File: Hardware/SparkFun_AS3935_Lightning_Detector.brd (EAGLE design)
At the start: 25.4 x 25.4 mm, 57 parts, among them U1 AS3935

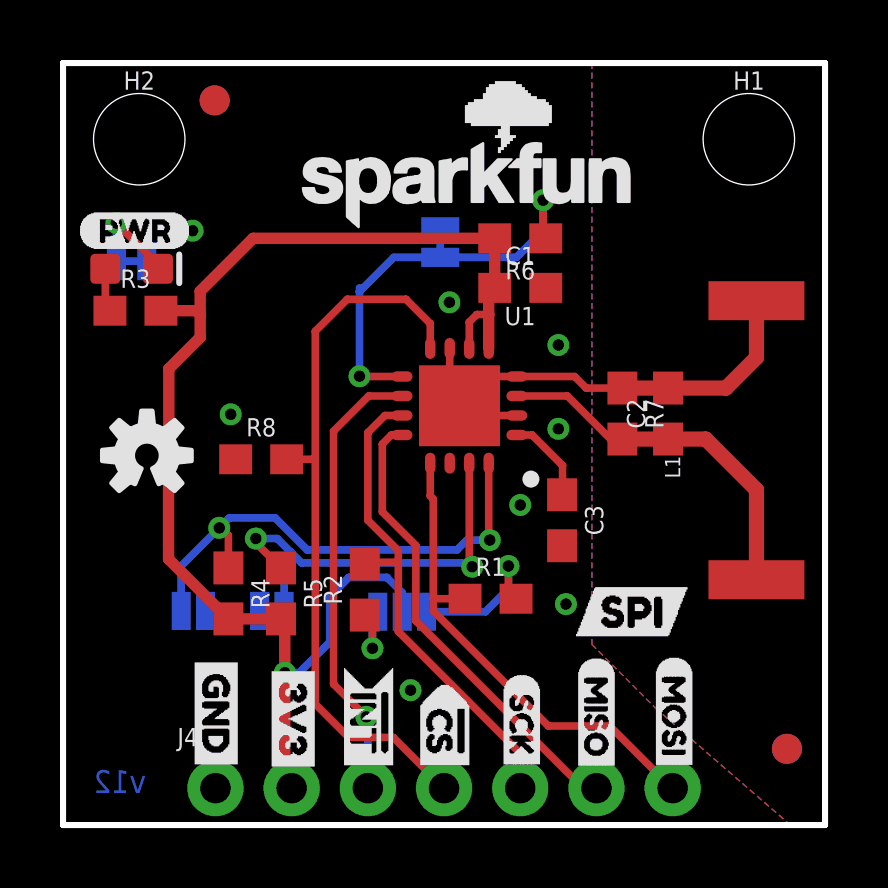
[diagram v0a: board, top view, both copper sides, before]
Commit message: Updates jumper on underside to read I2C rather than SPI
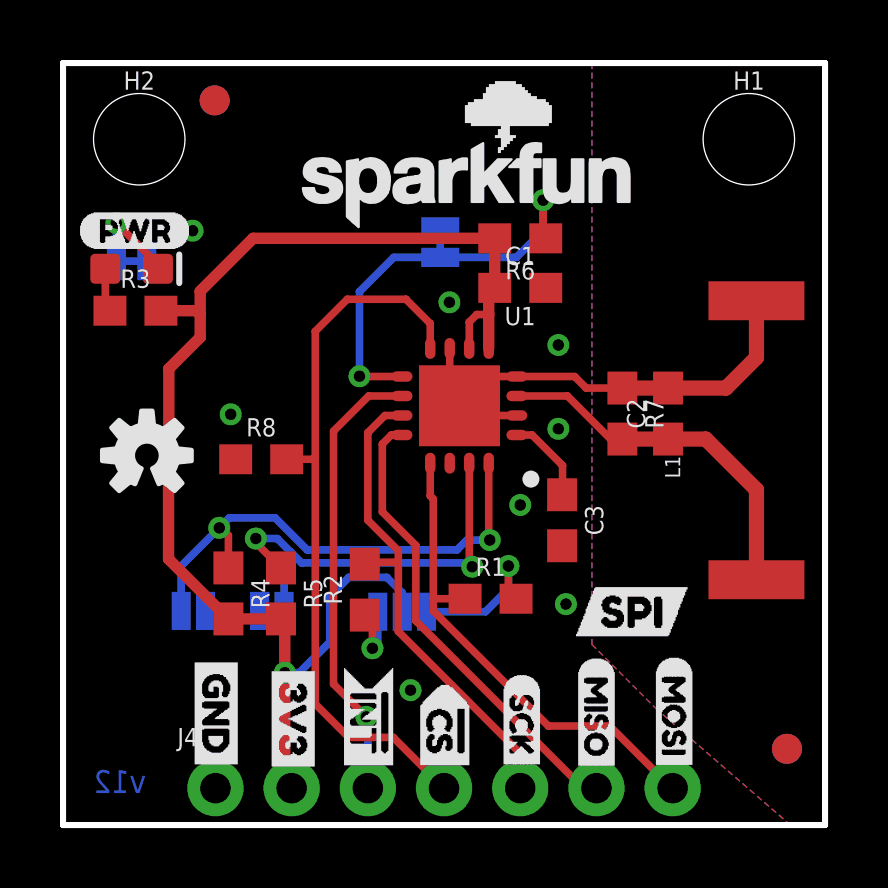
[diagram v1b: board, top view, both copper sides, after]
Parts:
- removed U$35: (no value), SPI:SPI0
- added U$16: (no value), Labels:I_SUPER2_C-()-04
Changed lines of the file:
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@@
 <layer number="19" name="Unrouted" color="6" fill="1" visible="yes" active="yes"/>
 <layer number="20" name="Dimension" color="15" fill="1" visible="yes" active="yes"/>
-<layer number="21" name="tPlace" color="16" fill="1" visible="no" active="yes"/>
-<layer number="22" name="bPlace" color="14" fill="1" visible="no" active="yes"/>
+<layer number="21" name="tPlace" color="16" fill="1" visible="yes" active="yes"/>
+<layer number="22" name="bPlace" color="14" fill="1" visible="yes" active="yes"/>
 <layer number="23" name="tOrigins" color="15" fill="1" visible="yes" active="yes"/>
 <layer number="24" name="bOrigins" color="15" fill="1" visible="yes" active="yes"/>
@@
 <element name="U$33" library="Labels" package="ADR-()-04" value="" x="7.9502" y="9.1694" smashed="yes" rot="MR0"/>
 <element name="U$34" library="PULLUP" package="I#C_PU0" value="" x="14.2494" y="9.144" smashed="yes" rot="MR0"/>
-<element name="U$35" library="SPI" package="SPI0" value="" x="14.605" y="21.717" smashed="yes" rot="MR0"/>
 <element name="U$36" library="one" package="10" value="" x="3.9878" y="7.0866" smashed="yes" rot="MR0"/>
 <element name="U$37" library="zero" package="00" value="" x="9.9822" y="7.1374" smashed="yes" rot="MR0"/>
@@
 <element name="U$14" library="INT" package="#INT0" value="" x="10.1854" y="5.5118" smashed="yes" rot="MR270"/>
 <element name="U$15" library="DataLines" package="SPI1" value="" x="21.082" y="7.112" smashed="yes" rot="MR0"/>
+<element name="U$16" library="Labels" package="I_SUPER2_C-()-04" value="" x="14.5034" y="21.6662" smashed="yes" rot="MR0"/>
 </elements>
 <signals>
@@
 <contactref element="U1" pad="9"/>
 <via x="16.002" y="20.828" extent="1-16" drill="0.381"/>
-<wire x1="15.2146" y1="19.0246" x2="15.24" y2="19.05" width="0.254" layer="16"/>
-<wire x1="15.24" y1="19.05" x2="16.002" y2="19.812" width="0.254" layer="16"/>
+<wire x1="15.113" y1="18.923" x2="16.002" y2="19.812" width="0.254" layer="16"/>
 <wire x1="16.002" y1="19.812" x2="16.002" y2="20.828" width="0.254" layer="16"/>
 <wire x1="16.09" y1="19.558" x2="16.002" y2="19.646" width="0.254" layer="1"/>
@@
 <via x="9.8806" y="14.9606" extent="1-16" drill="0.381"/>
 <wire x1="9.8806" y1="14.9606" x2="9.8806" y2="17.78" width="0.254" layer="16"/>
-<wire x1="9.8806" y1="17.78" x2="9.8806" y2="17.907" width="0.254" layer="16"/>
 <wire x1="9.8806" y1="17.78" x2="11.0236" y2="18.923" width="0.254" layer="16"/>
 <wire x1="11.0236" y1="18.923" x2="12.573" y2="18.923" width="0.254" layer="16"/>
 <wire x1="12.573" y1="18.923" x2="15.113" y2="18.923" width="0.254" layer="16"/>
-<wire x1="15.113" y1="18.923" x2="15.2146" y2="19.0246" width="0.254" layer="16"/>
 </signal>
 <signal name="MISO">
@@
 <wire x1="12.2396" y1="16.7164" x2="11.43" y2="17.526" width="0.254" layer="1"/>
 <wire x1="9.4742" y1="17.526" x2="11.43" y2="17.526" width="0.254" layer="1"/>
-<wire x1="7.3914" y1="12.192" x2="7.454" y2="12.192" width="0.254" layer="1"/>
 <wire x1="8.4074" y1="16.4592" x2="9.4742" y2="17.526" width="0.254" layer="1"/>
 <wire x1="8.4074" y1="4.0386" x2="8.4074" y2="12.192" width="0.254" layer="1"/>
@@
 <wire x1="10.0584" y1="6.9986" x2="10.3124" y2="6.7446" width="0.254" layer="1"/>
 <wire x1="10.3124" y1="6.7446" x2="10.3124" y2="5.8928" width="0.254" layer="1"/>
-<wire x1="10.4902" y1="7.112" x2="10.3124" y2="7.0866" width="0.254" layer="16"/>
-<wire x1="10.3124" y1="7.0866" x2="10.3124" y2="5.8928" width="0.254" layer="16"/>
+<wire x1="10.3124" y1="5.8928" x2="10.4902" y2="6.0706" width="0.254" layer="16"/>
+<wire x1="10.4902" y1="6.0706" x2="10.4902" y2="7.112" width="0.254" layer="16"/>
 </signal>
 <signal name="N$1">

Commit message: Fixes minor issues, changes i2c enable jumper label
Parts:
- removed U$16: (no value), Labels:I_SUPER2_C-()-04
- added U$17: (no value), i2c_EN:I#C_EN0
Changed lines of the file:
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@@
 <drawing>
 <settings>
-<setting alwaysvectorfont="no"/>
+<setting alwaysvectorfont="yes"/>
 <setting verticaltext="up"/>
 </settings>
@@
 <element name="U$14" library="INT" package="#INT0" value="" x="10.1854" y="5.5118" smashed="yes" rot="MR270"/>
 <element name="U$15" library="DataLines" package="SPI1" value="" x="21.082" y="7.112" smashed="yes" rot="MR0"/>
-<element name="U$16" library="Labels" package="I_SUPER2_C-()-04" value="" x="14.5034" y="21.6662" smashed="yes" rot="MR0"/>
+<element name="U$17" library="i2c_EN" package="I#C_EN0" value="" x="15.5194" y="21.6916" smashed="yes" rot="MR0"/>
 </elements>
 <signals>

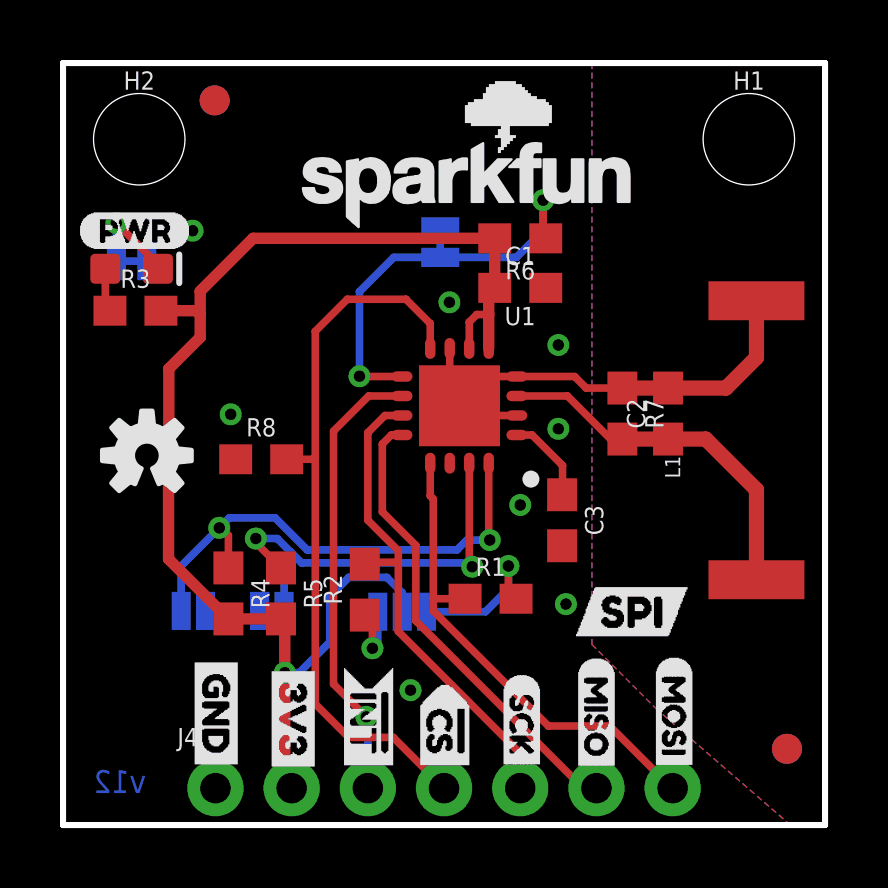
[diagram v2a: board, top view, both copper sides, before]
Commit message: Changes chip select pull down to pullup.
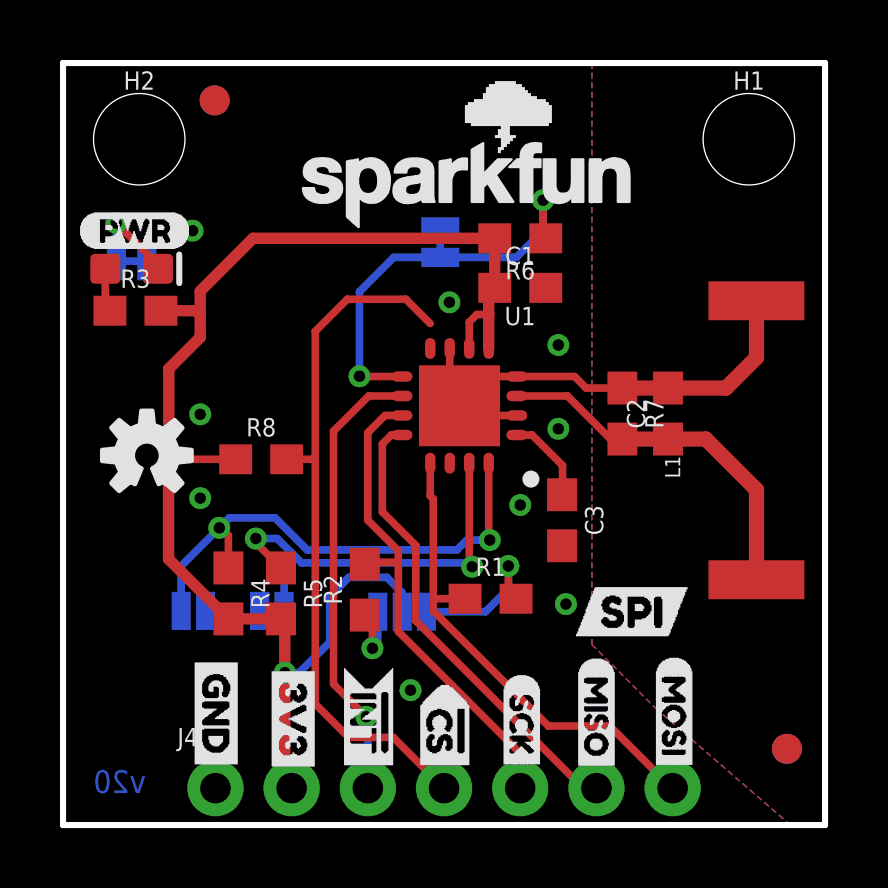
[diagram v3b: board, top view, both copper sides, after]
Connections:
- net 3.3V: now also R8.1
- net GND: no longer R8.1
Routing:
- net 3.3V: track 44.0 -> 46.2 mm
- net !CS: track 24.3 -> 23.4 mm
- net GND: vias 8 -> 9
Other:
- board text added: "v20"
- board text removed: "v12"
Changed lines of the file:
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@@
 <drawing>
 <settings>
-<setting alwaysvectorfont="yes"/>
+<setting alwaysvectorfont="no"/>
 <setting verticaltext="up"/>
 </settings>
-<grid distance="0.05" unitdist="inch" unit="inch" style="lines" multiple="1" display="yes" altdistance="0.001" altunitdist="inch" altunit="inch"/>
+<grid distance="0.01" unitdist="inch" unit="inch" style="lines" multiple="1" display="yes" altdistance="0.001" altunitdist="inch" altunit="inch"/>
 <layers>
 <layer number="1" name="Top" color="4" fill="1" visible="yes" active="yes"/>
@@
 <layer number="115" name="ReferenceISLANDS" color="7" fill="1" visible="no" active="no"/>
 <layer number="116" name="Patch_BOT" color="9" fill="4" visible="no" active="no"/>
-<layer number="117" name="PM_Ref" color="26" fill="1" visible="no" active="yes"/>
+<layer number="117" name="PM_Ref" color="26" fill="1" visible="yes" active="yes"/>
 <layer number="118" name="Rect_Pads" color="7" fill="1" visible="no" active="no"/>
-<layer number="119" name="PF_Ref" color="31" fill="1" visible="no" active="yes"/>
-<layer number="120" name="WFL_Ref" color="25" fill="1" visible="no" active="yes"/>
+<layer number="119" name="PF_Ref" color="31" fill="1" visible="yes" active="yes"/>
+<layer number="120" name="WFL_Ref" color="25" fill="1" visible="yes" active="yes"/>
 <layer number="121" name="_tsilk" color="7" fill="1" visible="no" active="no"/>
 <layer number="122" name="_bsilk" color="7" fill="1" visible="no" active="no"/>
@@
 <wire x1="0" y1="25.4" x2="0" y2="0" width="0.2032" layer="20"/>
 <text x="19.177" y="-19.177" size="1.778" layer="51" font="vector">Elias Santistevan</text>
-<text x="2.7686" y="1.0668" size="0.762" layer="16" font="vector" ratio="15" rot="MR0">v12</text>
+<text x="2.7686" y="1.0668" size="0.762" layer="16" font="vector" ratio="15" rot="MR0">v20</text>
 <dimension x1="25.4" y1="25.4" x2="0" y2="25.4" x3="12.7" y3="28.194" textsize="1.778" textratio="15" layer="47" dtype="horizontal" unit="inch"/>
 <dimension x1="25.4" y1="0" x2="25.4" y2="25.4" x3="30.226" y3="12.7" textsize="1.778" textratio="15" layer="47" dtype="horizontal" unit="inch"/>
@@
 <wire x1="12.8896" y1="15.8866" x2="12.8896" y2="14.3016" width="0.254" layer="1"/>
 <wire x1="12.8896" y1="14.3016" x2="13.2146" y2="13.9766" width="0.254" layer="1"/>
-<via x="5.588" y="13.6906" extent="1-16" drill="0.381"/>
+<via x="4.572" y="13.6906" extent="1-16" drill="0.381"/>
 <contactref element="JP5" pad="1"/>
 <via x="15.24" y="10.668" extent="1-16" drill="0.381"/>
@@
 <wire x1="22.098" y1="14.566" x2="23.114" y2="15.582" width="0.508" layer="1"/>
 <wire x1="23.114" y1="15.582" x2="23.114" y2="17.477" width="0.508" layer="1"/>
-<contactref element="R8" pad="1"/>
+<via x="4.572" y="10.8966" extent="1-16" drill="0.381"/>
 </signal>
 <signal name="3.3V">
@@
 <wire x1="7.3914" y1="6.7446" x2="7.2644" y2="6.8716" width="0.381" layer="1"/>
 <wire x1="5.5118" y1="6.8716" x2="3.517" y2="8.8664" width="0.381" layer="1"/>
-<wire x1="3.517" y1="8.8664" x2="3.517" y2="13.208" width="0.381" layer="1"/>
+<wire x1="3.517" y1="8.8664" x2="3.517" y2="12.192" width="0.381" layer="1"/>
+<wire x1="3.517" y1="12.192" x2="3.517" y2="13.208" width="0.381" layer="1"/>
 <wire x1="3.525" y1="13.2" x2="3.517" y2="13.208" width="0.381" layer="1"/>
 <via x="7.3914" y="5.08" extent="1-16" drill="0.381"/>
@@
 <wire x1="3.263" y1="17.145" x2="4.445" y2="17.145" width="0.381" layer="1"/>
 <wire x1="4.445" y1="17.145" x2="4.572" y2="17.018" width="0.381" layer="1"/>
+<contactref element="R8" pad="1"/>
+<wire x1="5.754" y1="12.192" x2="3.517" y2="12.192" width="0.254" layer="1"/>
 </signal>
 <signal name="MOSI/SDA">
@@
 <wire x1="11.008359375" y1="2.921" x2="9.525" y2="2.921" width="0.254" layer="1"/>
 <wire x1="9.525" y1="2.921" x2="8.4074" y2="4.0386" width="0.254" layer="1"/>
-<contactref element="U1" pad="8"/>
-<contactref element="R8" pad="2"/>
-<wire x1="12.2396" y1="15.8866" x2="12.2396" y2="16.7164" width="0.254" layer="1"/>
 <wire x1="12.2396" y1="16.7164" x2="11.43" y2="17.526" width="0.254" layer="1"/>
 <wire x1="9.4742" y1="17.526" x2="11.43" y2="17.526" width="0.254" layer="1"/>
@@
 <wire x1="8.4074" y1="4.0386" x2="8.4074" y2="12.192" width="0.254" layer="1"/>
 <wire x1="8.4074" y1="12.192" x2="8.4074" y2="16.4592" width="0.254" layer="1"/>
+<contactref element="U1" pad="8"/>
+<contactref element="R8" pad="2"/>
 <wire x1="7.454" y1="12.192" x2="8.4074" y2="12.192" width="0.254" layer="1"/>
+<wire x1="12.2396" y1="16.7164" x2="12.2396" y2="15.8866" width="0" layer="19" extent="1-1"/>
 </signal>
 <signal name="N$2">
